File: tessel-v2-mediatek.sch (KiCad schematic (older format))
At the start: 51 parts, among them U201 MT7620N, X201 20MHz

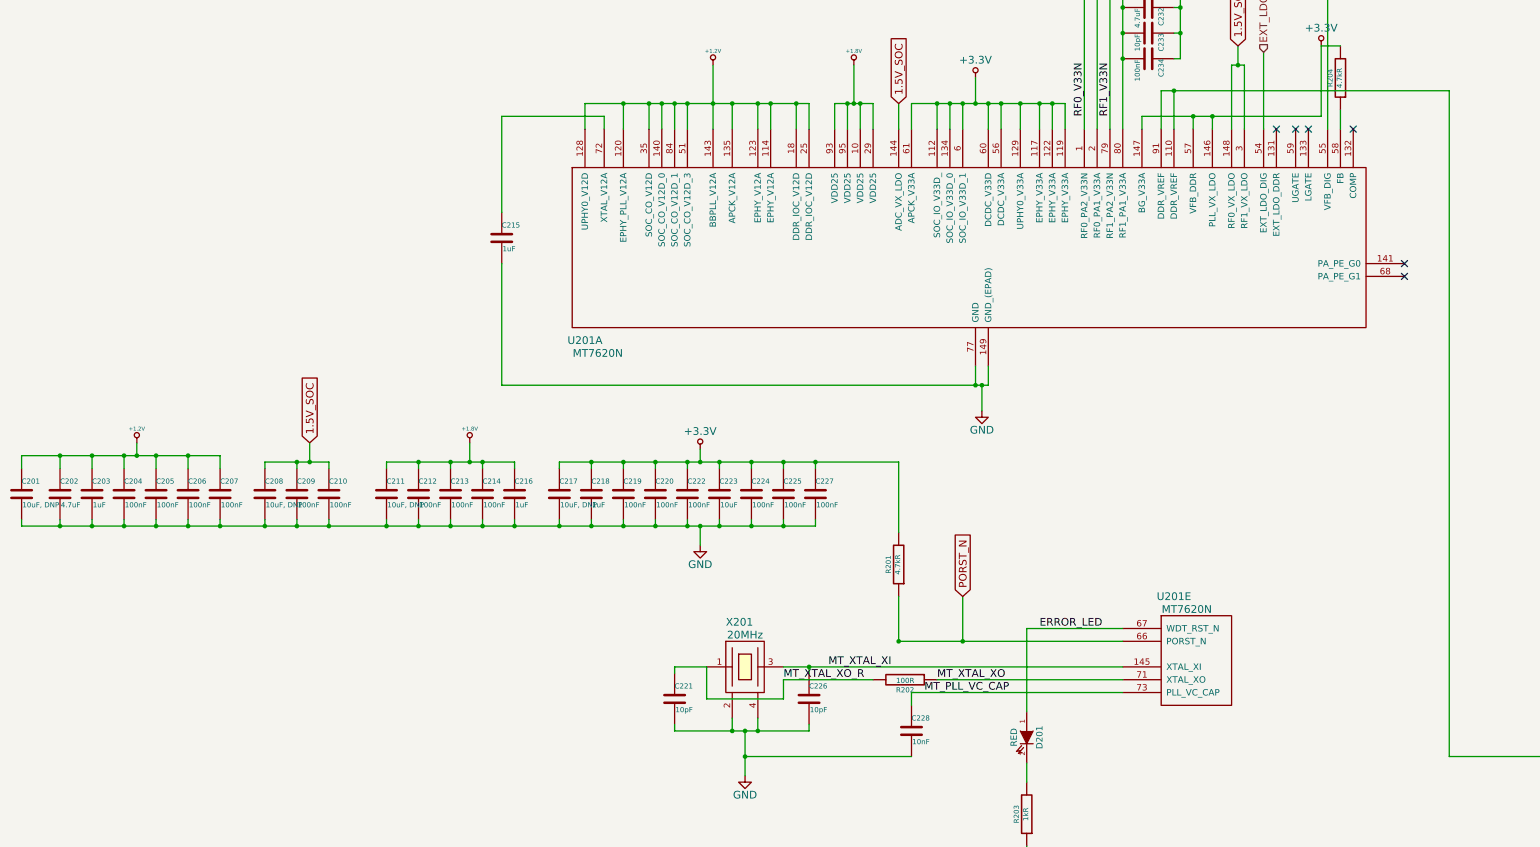
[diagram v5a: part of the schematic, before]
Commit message: swapped to "X DNP" from "X, DNP"; reassign and whatnot
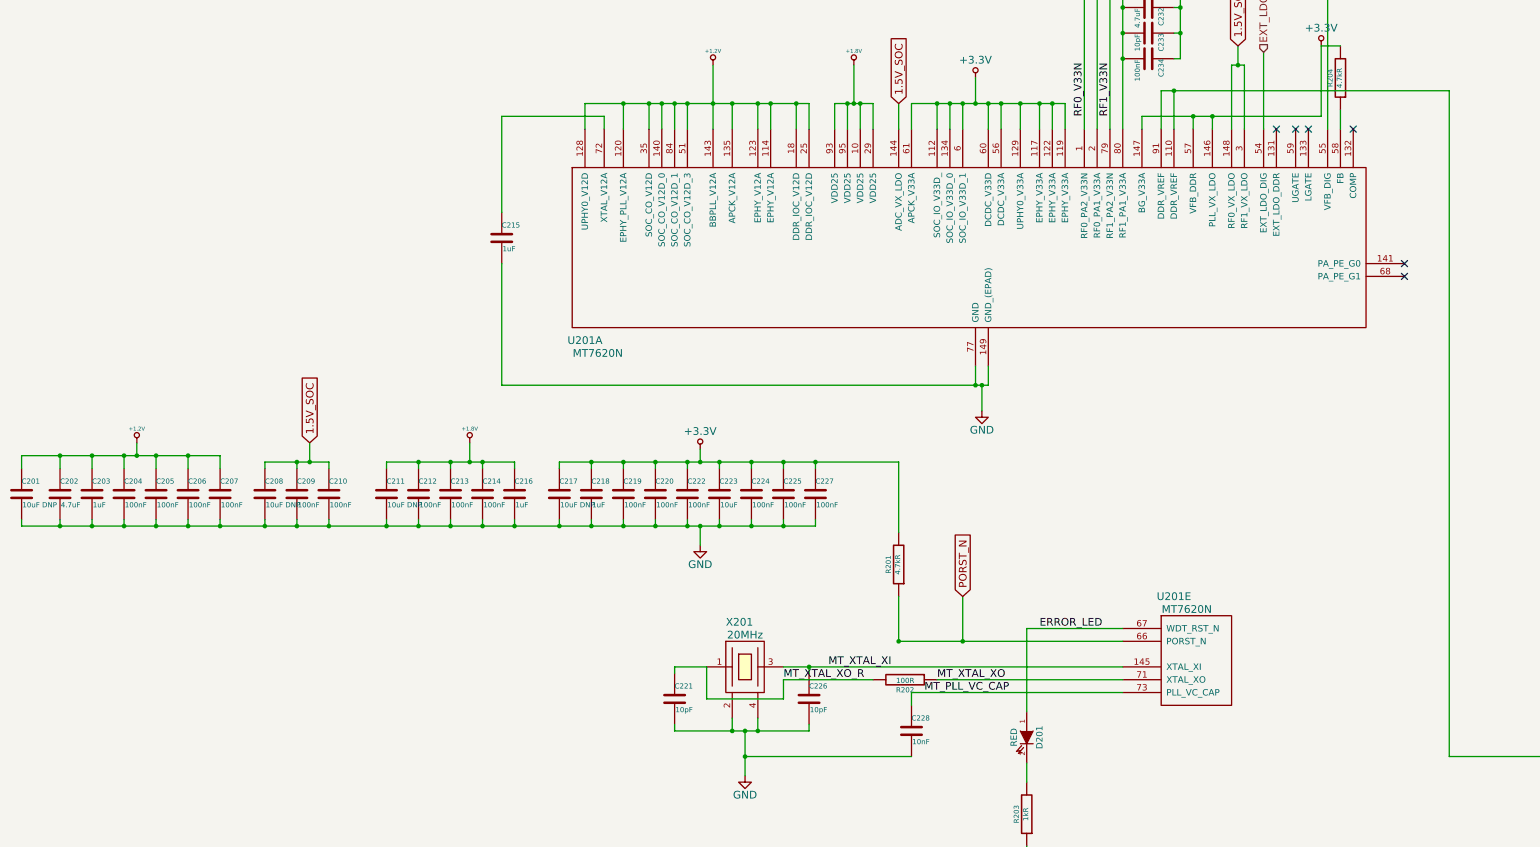
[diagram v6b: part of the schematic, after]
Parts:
- C201, C208, C211, C217: value 10uF, DNP -> 10uF DNP
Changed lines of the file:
@@
 $EndComp
 $Comp
-L GND #PWR209
+L GND #PWR01
 U 1 1 548FCCAF
 P 8550 7950
-F 0 "#PWR209" H 8550 7700 60  0001 C CNN
+F 0 "#PWR01" H 8550 7700 60  0001 C CNN
 F 1 "GND" H 8550 7800 60  0000 C CNN
 F 2 "" H 8550 7950 60  0000 C CNN
@@
 $EndComp
 $Comp
-L GND #PWR206
+L GND #PWR02
 U 1 1 548FD1CD
 P 6700 10800
-F 0 "#PWR206" H 6700 10550 60  0001 C CNN
+F 0 "#PWR02" H 6700 10550 60  0001 C CNN
 F 1 "GND" H 6700 10650 60  0000 C CNN
 F 2 "" H 6700 10800 60  0000 C CNN
@@
 $EndComp
 $Comp
-L +3.3V #PWR208
+L +3.3V #PWR03
 U 1 1 548FF520
 P 8500 5350
-F 0 "#PWR208" H 8500 5200 60  0001 C CNN
+F 0 "#PWR03" H 8500 5200 60  0001 C CNN
 F 1 "+3.3V" H 8500 5490 60  0000 C CNN
 F 2 "" H 8500 5350 60  0000 C CNN
@@
 $EndComp
 $Comp
-L +3.3V #PWR211
+L +3.3V #PWR04
 U 1 1 548FF90D
 P 9450 3850
-F 0 "#PWR211" H 9450 3700 60  0001 C CNN
+F 0 "#PWR04" H 9450 3700 60  0001 C CNN
 F 1 "+3.3V" H 9450 3990 60  0000 C CNN
 F 2 "" H 9450 3850 60  0000 C CNN
@@
 $EndComp
 $Comp
-L GND #PWR212
+L GND #PWR05
 U 1 1 548FFC28
 P 10100 4650
-F 0 "#PWR212" H 10100 4400 60  0001 C CNN
+F 0 "#PWR05" H 10100 4400 60  0001 C CNN
 F 1 "GND" H 10100 4500 60  0000 C CNN
 F 2 "" H 10100 4650 60  0000 C CNN
@@
 NoConn ~ 11450 5750
 $Comp
-L +3.3V #PWR213
+L +3.3V #PWR06
 U 1 1 54901F95
 P 11200 5100
-F 0 "#PWR213" H 11200 4950 60  0001 C CNN
+F 0 "#PWR06" H 11200 4950 60  0001 C CNN
 F 1 "+3.3V" H 11200 5240 60  0000 C CNN
 F 2 "" H 11200 5100 60  0000 C CNN
@@
 $EndComp
 $Comp
-L +3.3V #PWR203
+L +3.3V #PWR07
 U 1 1 54903A33
 P 6350 8250
-F 0 "#PWR203" H 6350 8100 60  0001 C CNN
+F 0 "#PWR07" H 6350 8100 60  0001 C CNN
 F 1 "+3.3V" H 6350 8390 60  0000 C CNN
 F 2 "" H 6350 8250 60  0000 C CNN
@@
 $EndComp
 $Comp
-L GND #PWR204
+L GND #PWR08
 U 1 1 54903B07
 P 6350 9000
-F 0 "#PWR204" H 6350 8750 60  0001 C CNN
+F 0 "#PWR08" H 6350 8750 60  0001 C CNN
 F 1 "GND" H 6350 8850 60  0000 C CNN
 F 2 "" H 6350 9000 60  0000 C CNN
@@
 $EndComp
 $Comp
-L +1.2V #PWR205
+L +1.2V #PWR09
 U 1 1 5490938C
 P 6450 5250
-F 0 "#PWR205" H 6450 5390 20  0001 C CNN
+F 0 "#PWR09" H 6450 5390 20  0001 C CNN
 F 1 "+1.2V" H 6450 5360 30  0000 C CNN
 F 2 "" H 6450 5250 60  0000 C CNN
@@
 $EndComp
 $Comp
-L +1.8V #PWR207
+L +1.8V #PWR010
 U 1 1 549093A0
 P 7550 5250
-F 0 "#PWR207" H 7550 5390 20  0001 C CNN
+F 0 "#PWR010" H 7550 5390 20  0001 C CNN
 F 1 "+1.8V" H 7550 5360 30  0000 C CNN
 F 2 "" H 7550 5250 60  0000 C CNN
@@
 $EndComp
 $Comp
-L +1.8V #PWR202
+L +1.8V #PWR011
 U 1 1 5490A3FA
 P 4550 8200
-F 0 "#PWR202" H 4550 8340 20  0001 C CNN
+F 0 "#PWR011" H 4550 8340 20  0001 C CNN
 F 1 "+1.8V" H 4550 8310 30  0000 C CNN
 F 2 "" H 4550 8200 60  0000 C CNN
@@
 $EndComp
 $Comp
-L +1.2V #PWR201
+L +1.2V #PWR012
 U 1 1 5490A9A8
 P 1950 8200
-F 0 "#PWR201" H 1950 8340 20  0001 C CNN
+F 0 "#PWR012" H 1950 8340 20  0001 C CNN
 F 1 "+1.2V" H 1950 8310 30  0000 C CNN
 F 2 "" H 1950 8200 60  0000 C CNN
@@
 $EndComp
 $Comp
-L +3.3V #PWR217
+L +3.3V #PWR013
 U 1 1 5490FE7F
 P 13500 2100
-F 0 "#PWR217" H 13500 1950 60  0001 C CNN
+F 0 "#PWR013" H 13500 1950 60  0001 C CNN
 F 1 "+3.3V" H 13500 2240 60  0000 C CNN
 F 2 "" H 13500 2100 60  0000 C CNN
@@
 $EndComp
 $Comp
-L GND #PWR215
+L GND #PWR014
 U 1 1 54910029
 P 12750 2900
-F 0 "#PWR215" H 12750 2650 60  0001 C CNN
+F 0 "#PWR014" H 12750 2650 60  0001 C CNN
 F 1 "GND" H 12750 2750 60  0000 C CNN
 F 2 "" H 12750 2900 60  0000 C CNN
@@
 $EndComp
 $Comp
-L +3.3V #PWR218
+L +3.3V #PWR015
 U 1 1 54910D64
 P 13500 3150
-F 0 "#PWR218" H 13500 3000 60  0001 C CNN
+F 0 "#PWR015" H 13500 3000 60  0001 C CNN
 F 1 "+3.3V" H 13500 3290 60  0000 C CNN
 F 2 "" H 13500 3150 60  0000 C CNN
@@
 $EndComp
 $Comp
-L GND #PWR216
+L GND #PWR016
 U 1 1 54910D6B
 P 12750 3950
-F 0 "#PWR216" H 12750 3700 60  0001 C CNN
+F 0 "#PWR016" H 12750 3700 60  0001 C CNN
 F 1 "GND" H 12750 3800 60  0000 C CNN
 F 2 "" H 12750 3950 60  0000 C CNN
@@
 $EndComp
 $Comp
-L +1.2V #PWR214
+L +1.2V #PWR017
 U 1 1 5491253A
 P 11250 4700
-F 0 "#PWR214" H 11250 4840 20  0001 C CNN
+F 0 "#PWR017" H 11250 4840 20  0001 C CNN
 F 1 "+1.2V" H 11250 4810 30  0000 C CNN
 F 2 "" H 11250 4700 60  0000 C CNN
@@
 P 1050 8600
 F 0 "C201" H 1050 8700 40  0000 L CNN
-F 1 "10uF, DNP" H 1056 8515 40  0000 L CNN
+F 1 "10uF DNP" H 1056 8515 40  0000 L CNN
 F 2 "SMD_Packages:SMD-0805" H 1088 8450 30  0001 C CNN
 F 3 "" H 1050 8600 60  0000 C CNN
@@
 P 2950 8600
 F 0 "C208" H 2950 8700 40  0000 L CNN
-F 1 "10uF, DNP" H 2956 8515 40  0000 L CNN
+F 1 "10uF DNP" H 2956 8515 40  0000 L CNN
 F 2 "SMD_Packages:SMD-0805" H 2988 8450 30  0001 C CNN
 F 3 "" H 2950 8600 60  0000 C CNN
@@
 P 3900 8600
 F 0 "C211" H 3900 8700 40  0000 L CNN
-F 1 "10uF, DNP" H 3906 8515 40  0000 L CNN
+F 1 "10uF DNP" H 3906 8515 40  0000 L CNN
 F 2 "SMD_Packages:SMD-0805" H 3938 8450 30  0001 C CNN
 F 3 "" H 3900 8600 60  0000 C CNN
@@
 P 5250 8600
 F 0 "C217" H 5250 8700 40  0000 L CNN
-F 1 "10uF, DNP" H 5256 8515 40  0000 L CNN
+F 1 "10uF DNP" H 5256 8515 40  0000 L CNN
 F 2 "SMD_Packages:SMD-0805" H 5288 8450 30  0001 C CNN
 F 3 "" H 5250 8600 60  0000 C CNN
@@
 	17300 10650 12200 10650
 Wire Wire Line
-	12200 5450 12200 10650
-Wire Wire Line
-	9950 5450 12200 5450
+	12200 10650 12200 5450
+Wire Wire Line
+	12200 5450 9950 5450
 Wire Wire Line
 	9950 5450 9950 5750
@@
 F 0 "D201" H 8900 10600 50  0000 C CNN
 F 1 "RED" H 8900 10400 50  0000 C CNN
-F 2 "" H 8900 10500 60  0000 C CNN
+F 2 "" H 8900 10500 60  0001 C CNN
 F 3 "" H 8900 10500 60  0000 C CNN
 	1    8900 10500
@@
 	8900 10850 8900 10700
 $Comp
-L GND #PWR210
+L GND #PWR018
 U 1 1 54BF57E4
 P 8900 11450
-F 0 "#PWR210" H 8900 11200 60  0001 C CNN
+F 0 "#PWR018" H 8900 11200 60  0001 C CNN
 F 1 "GND" H 8900 11300 60  0000 C CNN
 F 2 "" H 8900 11450 60  0000 C CNN

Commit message: datasheets, refdes, netlists, and component mappings
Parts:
- D201: footprint (none) -> LEDs:LED-0603
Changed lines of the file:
@@
 F 0 "D201" H 8900 10600 50  0000 C CNN
 F 1 "RED" H 8900 10400 50  0000 C CNN
-F 2 "" H 8900 10500 60  0001 C CNN
+F 2 "LEDs:LED-0603" H 8900 10500 60  0001 C CNN
 F 3 "" H 8900 10500 60  0000 C CNN
 	1    8900 10500

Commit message: more cp things, 33cp is in place
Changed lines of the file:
@@
 MT_SO
 Text HLabel 19850 8050 2    60   Input ~ 0
-MT_CS
+MT_CS0
 Text HLabel 19850 8200 2    60   Input ~ 0
 MT_SCK
